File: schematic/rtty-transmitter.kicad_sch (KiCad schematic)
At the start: 32 parts, among them J1 USB_B, J2 USBasp header, J3 Conn_Coaxial, Q1 PN2222A, U1 MCP2221AxP, U2 ATmega328P-P, U3 MCP4901, U4 MCP6022, U5 2x5 Pin Header Connector Fema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, U6 25LC1024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

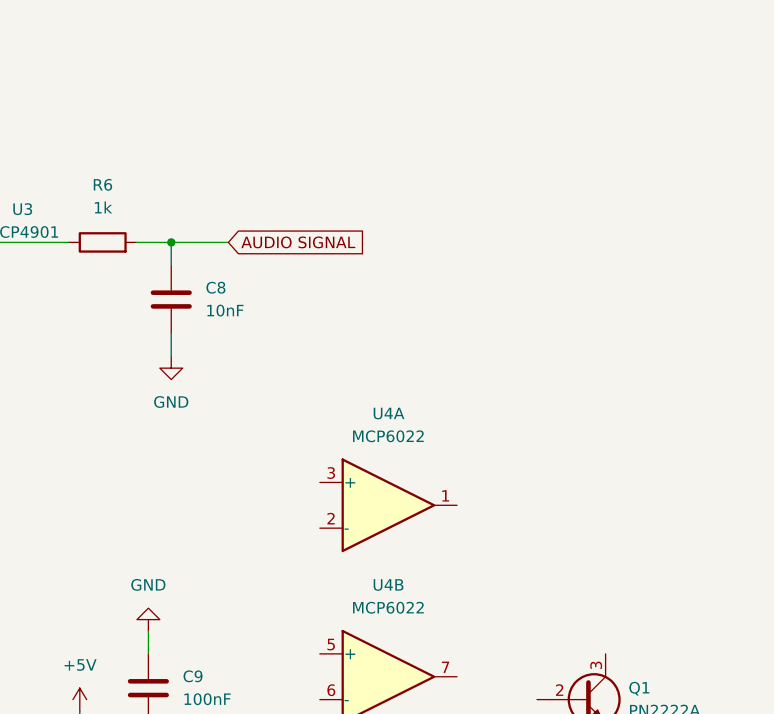
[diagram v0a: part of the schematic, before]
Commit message: High-pass filter added after DAC output to remove DC offset
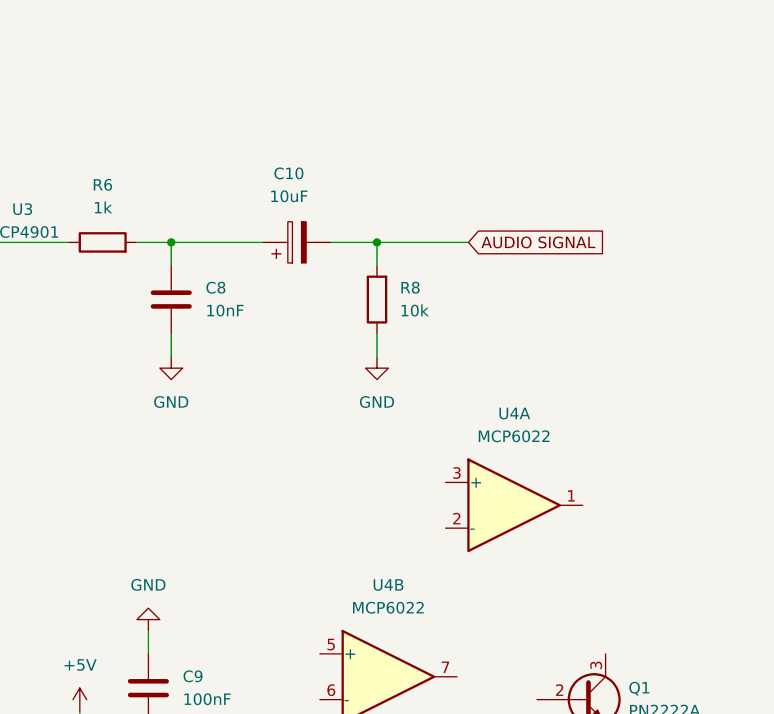
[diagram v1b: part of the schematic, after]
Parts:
- added C10: 10uF, Capacitor_THT:CP_Radial_D6.3mm_P2.50mm, symbol Device:C_Polarized
- added R8: 10k, StockLib:R_10k_Axial_DIN0207, symbol StockLib:R_10k
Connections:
- net AUDIO SIGNAL: now also C10.2, R8.2; no longer C8.2, R6.2
- net GND: now also R8.1
- new net: C10.1, C8.2, R6.2
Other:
- moved on the sheet: U4A
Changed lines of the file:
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@@
   (junction (at 168.91 86.36) (diameter 0) (color 0 0 0 0)
   )
+  (junction (at 245.11 48.26) (diameter 0) (color 0 0 0 0)
+  )
+  (junction (at 222.25 48.26) (diameter 0) (color 0 0 0 0)
+  )
   (junction (at 200.66 109.22) (diameter 0) (color 0 0 0 0)
   )
@@
   )
   (junction (at 182.88 113.03) (diameter 0) (color 0 0 0 0)
-  )
-  (junction (at 222.25 48.26) (diameter 0) (color 0 0 0 0)
   )
   (junction (at 162.56 69.85) (diameter 0) (color 0 0 0 0)
@@
     (stroke (width 0) (type default))
   )
+  (wire (pts (xy 245.11 48.26) (xy 255.27 48.26))
+    (stroke (width 0) (type default))
+  )
   (wire (pts (xy 128.27 123.19) (xy 128.27 125.73))
     (stroke (width 0) (type default))
@@
     (stroke (width 0) (type default))
   )
+  (wire (pts (xy 222.25 48.26) (xy 232.41 48.26))
+    (stroke (width 0) (type default))
+  )
   (wire (pts (xy 143.51 97.79) (xy 151.13 97.79))
     (stroke (width 0) (type default))
@@
     (stroke (width 0) (type default))
   )
-  (wire (pts (xy 222.25 48.26) (xy 228.6 48.26))
-    (stroke (width 0) (type default))
-  )
   (wire (pts (xy 60.96 46.99) (xy 66.04 46.99))
     (stroke (width 0) (type default))
@@
     (stroke (width 0) (type default))
   )
+  (wire (pts (xy 240.03 48.26) (xy 245.11 48.26))
+    (stroke (width 0) (type default))
+  )
   (wire (pts (xy 156.21 59.69) (xy 156.21 48.26))
     (stroke (width 0) (type default))
@@
     (stroke (width 0) (type default))
   )
+  (wire (pts (xy 245.11 48.26) (xy 245.11 50.8))
+    (stroke (width 0) (type default))
+  )
   (wire (pts (xy 193.04 129.54) (xy 193.04 97.79))
     (stroke (width 0) (type default))
@@
   )
   (wire (pts (xy 80.01 114.3) (xy 91.44 114.3))
+    (stroke (width 0) (type default))
+  )
+  (wire (pts (xy 245.11 58.42) (xy 245.11 60.96))
     (stroke (width 0) (type default))
   )
@@
     )
   )
-  (global_label "AUDIO SIGNAL" (shape input) (at 228.6 48.26 0) (fields_autoplaced)
+  (global_label "AUDIO SIGNAL" (shape input) (at 255.27 48.26 0) (fields_autoplaced)
     (effects (font (size 1.27 1.27)) (justify left))
-    (property "Intersheetrefs" "${INTERSHEET_REFS}" (at 244.7087 48.26 0)
+    (property "Intersheetrefs" "${INTERSHEET_REFS}" (at 271.3787 48.26 0)
       (effects (font (size 1.27 1.27)) (justify left) hide)
     )
@@
     )
   )
-  (symbol (lib_id "Amplifier_Operational:MCP6022") (at 246.38 77.47 0) (unit 1)
-    (in_bom yes) (on_board yes) (dnp no) (fields_autoplaced)
-    (property "Reference" "U4" (at 246.38 67.31 0)
-      (effects (font (size 1.27 1.27)))
-    )
-    (property "Value" "MCP6022" (at 246.38 69.85 0)
-      (effects (font (size 1.27 1.27)))
-    )
-    (property "Footprint" "Package_DIP:DIP-8_W7.62mm" (at 246.38 77.47 0)
-      (effects (font (size 1.27 1.27)) hide)
-    )
-    (property "Datasheet" "http://ww1.microchip.com/downloads/en/devicedoc/20001685e.pdf" (at 246.38 77.47 0)
+  (symbol (lib_id "Amplifier_Operational:MCP6022") (at 260.35 77.47 0) (unit 1)
+    (in_bom yes) (on_board yes) (dnp no) (fields_autoplaced)
+    (property "Reference" "U4" (at 260.35 67.31 0)
+      (effects (font (size 1.27 1.27)))
+    )
+    (property "Value" "MCP6022" (at 260.35 69.85 0)
+      (effects (font (size 1.27 1.27)))
+    )
+    (property "Footprint" "Package_DIP:DIP-8_W7.62mm" (at 260.35 77.47 0)
+      (effects (font (size 1.27 1.27)) hide)
+    )
+    (property "Datasheet" "http://ww1.microchip.com/downloads/en/devicedoc/20001685e.pdf" (at 260.35 77.47 0)
       (effects (font (size 1.27 1.27)) hide)
     )
@@
     )
   )
+  (symbol (lib_id "power:GND") (at 245.11 60.96 0) (unit 1)
+    (in_bom yes) (on_board yes) (dnp no) (fields_autoplaced)
+    (property "Reference" "#PWR033" (at 245.11 67.31 0)
+      (effects (font (size 1.27 1.27)) hide)
+    )
+    (property "Value" "GND" (at 245.11 66.04 0)
+      (effects (font (size 1.27 1.27)))
+    )
+    (property "Footprint" "" (at 245.11 60.96 0)
+      (effects (font (size 1.27 1.27)) hide)
+    )
+    (property "Datasheet" "" (at 245.11 60.96 0)
+      (effects (font (size 1.27 1.27)) hide)
+    )
+    (pin "1")
+    (instances
+      (project "rtty-transmitter"
+        (path "/4ea8d87c-4bb0-4c80-84f6-8dbfd2cdcfd6"
+          (reference "#PWR033") (unit 1)
+        )
+      )
+    )
+  )
   (symbol (lib_id "StockLib:LED 5mm YELLOW") (at 62.23 114.3 0) (unit 1)
     (in_bom yes) (on_board yes) (dnp no) (fields_autoplaced)
@@
     )
   )
+  (symbol (lib_id "Device:C_Polarized") (at 236.22 48.26 90) (unit 1)
+    (in_bom yes) (on_board yes) (dnp no) (fields_autoplaced)
+    (property "Reference" "C10" (at 235.331 40.64 90)
+      (effects (font (size 1.27 1.27)))
+    )
+    (property "Value" "10uF" (at 235.331 43.18 90)
+      (effects (font (size 1.27 1.27)))
+    )
+    (property "Footprint" "Capacitor_THT:CP_Radial_D6.3mm_P2.50mm" (at 240.03 47.2948 0)
+      (effects (font (size 1.27 1.27)) hide)
+    )
+    (property "Datasheet" "~" (at 236.22 48.26 0)
+      (effects (font (size 1.27 1.27)) hide)
+    )
+    (pin "1")
+    (pin "2")
+    (instances
+      (project "rtty-transmitter"
+        (path "/4ea8d87c-4bb0-4c80-84f6-8dbfd2cdcfd6"
+          (reference "C10") (unit 1)
+        )
+      )
+    )
+  )
   (symbol (lib_id "power:GND") (at 171.45 45.72 270) (unit 1)
     (in_bom yes) (on_board yes) (dnp no) (fields_autoplaced)
@@
         )
       )
+    )
+  )
+  (symbol (lib_id "StockLib:R_10k") (at 245.11 54.61 180) (unit 1)
+    (in_bom yes) (on_board yes) (dnp no) (fields_autoplaced)
+    (property "Reference" "R8" (at 247.65 53.34 0)
+      (effects (font (size 1.27 1.27)) (justify right))
+    )
+    (property "Value" "10k" (at 247.65 55.88 0)
+      (effects (font (size 1.27 1.27)) (justify right))
+    )
+    (property "Footprint" "StockLib:R_10k_Axial_DIN0207" (at 246.888 54.61 90)
+      (effects (font (size 1.27 1.27)) hide)
+    )
+    (property "Datasheet" "~" (at 245.11 54.61 0)
+      (effects (font (size 1.27 1.27)) hide)
+    )
+    (pin "1")
+    (pin "2")
+    (instances
+      (project "rtty-transmitter"
+        (path "/4ea8d87c-4bb0-4c80-84f6-8dbfd2cdcfd6"
+          (reference "R8") (unit 1)
+        )
+      )

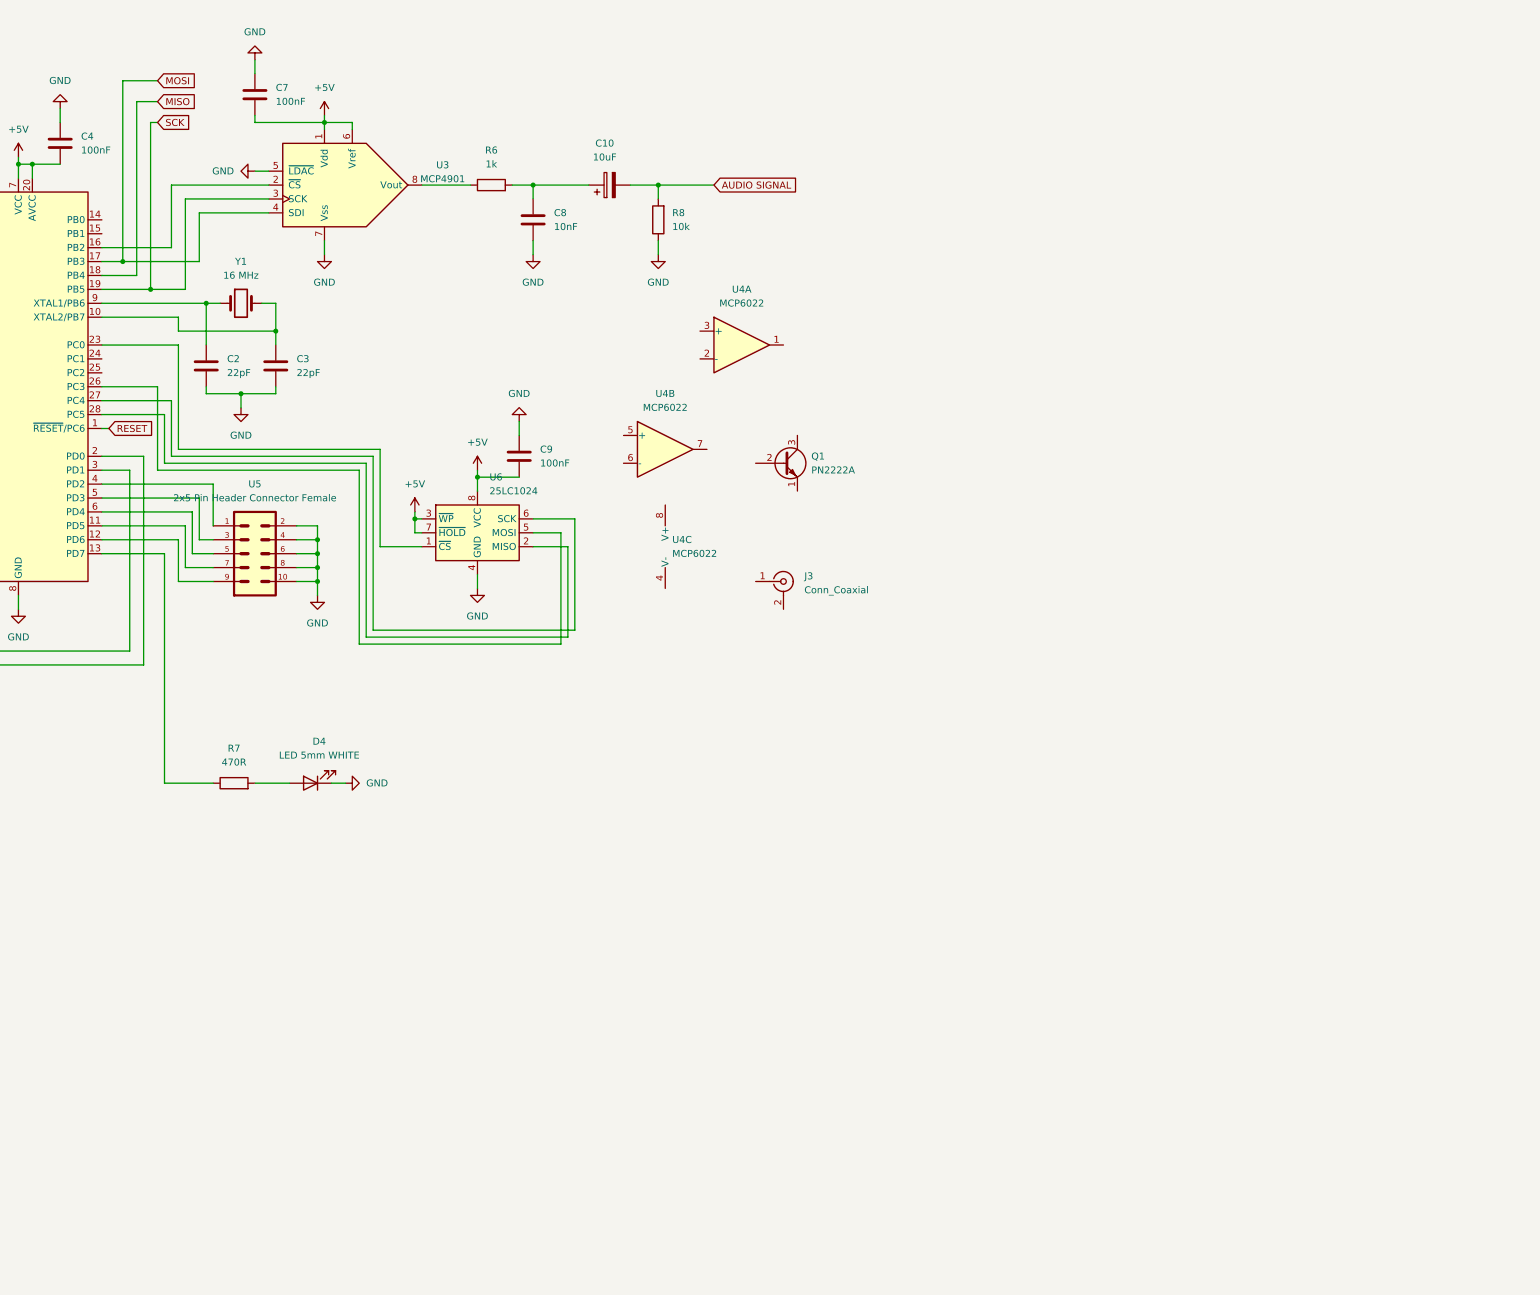
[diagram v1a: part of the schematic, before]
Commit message: Antenna amplifier and modulator-mixer added (current-modulated cascode amplifier), op-amp base circuits added
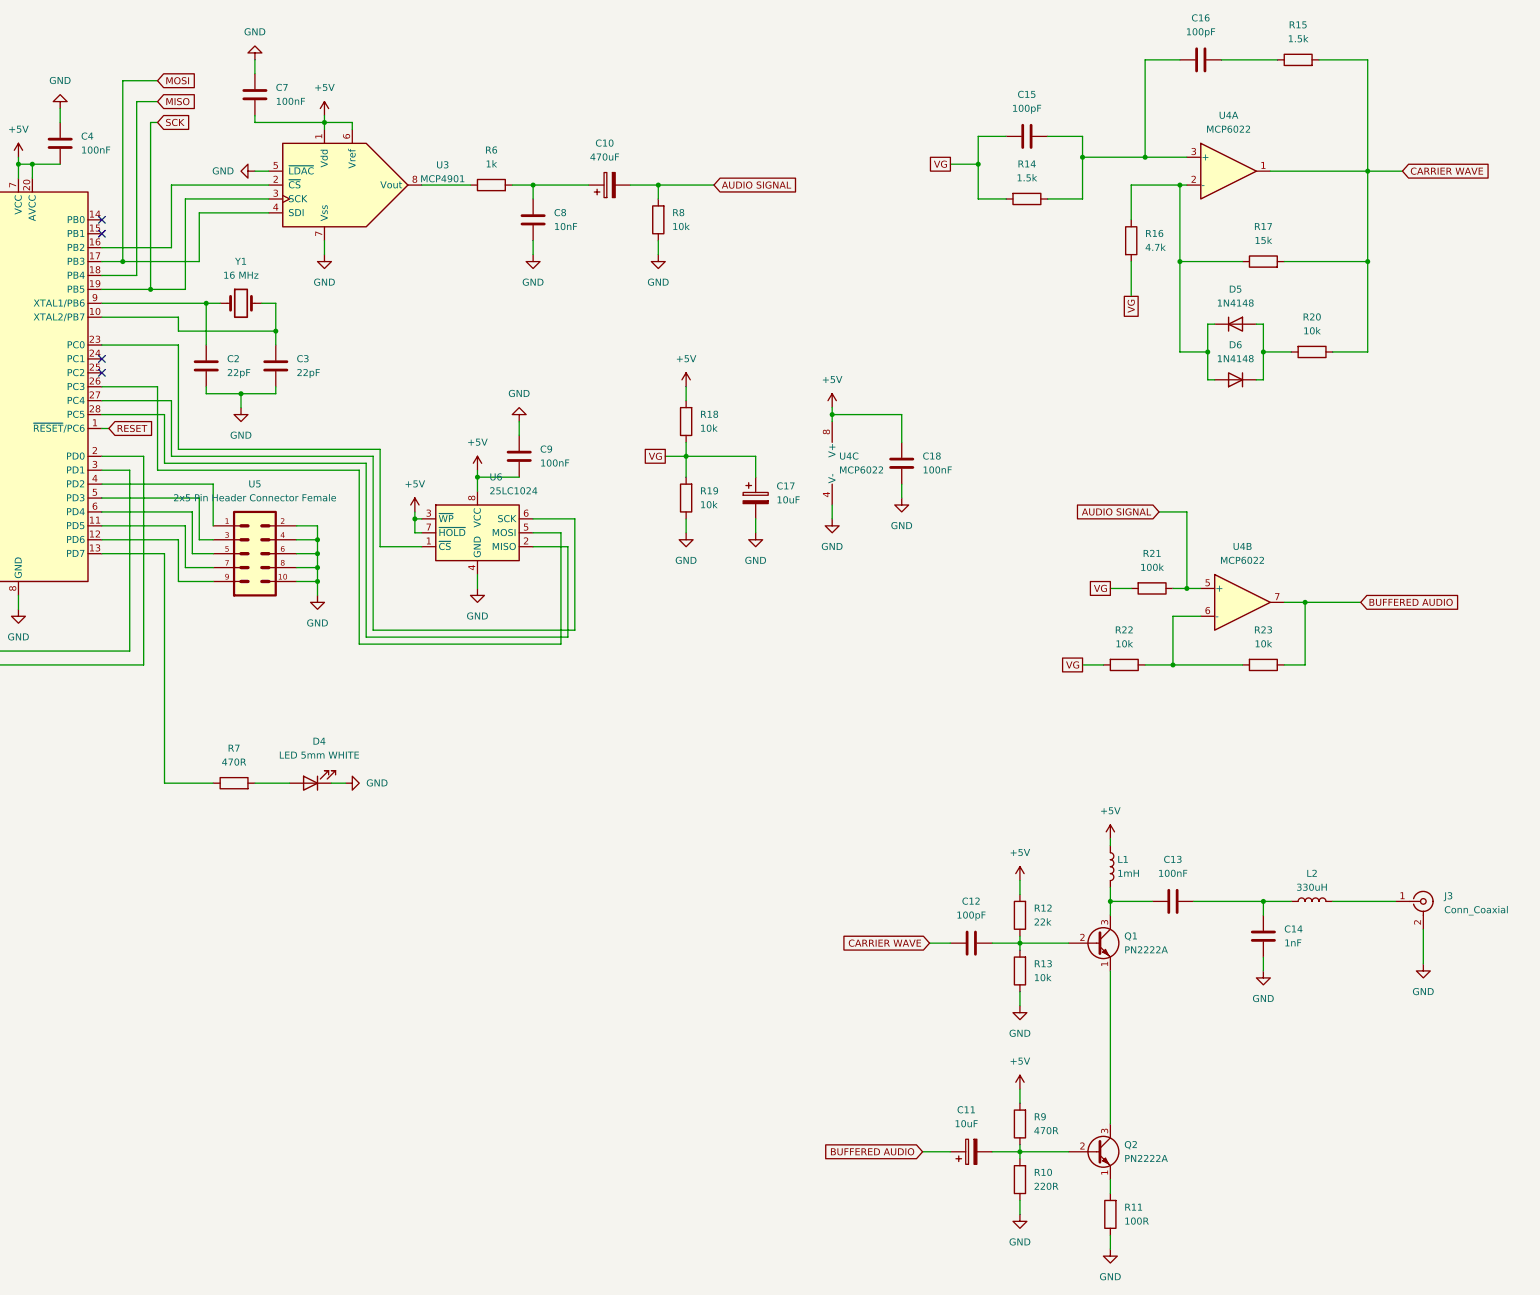
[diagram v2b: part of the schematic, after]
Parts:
- added C11, C17: 10uF, Capacitor_THT:CP_Radial_D6.3mm_P2.50mm, symbol Device:C_Polarized
- added C12, C15, C16: 100pF, Capacitor_THT:C_Disc_D3.0mm_W1.6mm_P2.50mm, symbol Device:C
- added C13, C18: 100nF, StockLib:C_100nF_L7.0mm_W2.5mm_P5.00mm, symbol StockLib:C_100nF
- added C14: 1nF, Capacitor_THT:C_Disc_D3.0mm_W1.6mm_P2.50mm, symbol Device:C
- added D5, D6: 1N4148, Diode_THT:D_DO-35_SOD27_P7.62mm_Horizontal, symbol StockLib:1N4148
- added L1: 1mH, Inductor_THT:L_Radial_D8.7mm_P5.00mm_Fastron_07HCP, symbol StockLib:L
- added L2: 330uH, Inductor_THT:L_Radial_D8.7mm_P5.00mm_Fastron_07HCP, symbol StockLib:L
- added Q2: PN2222A, Package_TO_SOT_THT:TO-92_Inline, symbol StockLib:PN2222A
- added R10: 220R, StockLib:R_10k_Axial_DIN0207, symbol StockLib:R_10k
- added R11: 100R, StockLib:R_10k_Axial_DIN0207, symbol StockLib:R_10k
- added R12: 22k, StockLib:R_10k_Axial_DIN0207, symbol StockLib:R_10k
- added R13, R18, R19, R20, R22, R23: 10k, StockLib:R_10k_Axial_DIN0207, symbol StockLib:R_10k
- added R14, R15: 1.5k, StockLib:R_10k_Axial_DIN0207, symbol StockLib:R_10k
- added R16: 4.7k, StockLib:R_10k_Axial_DIN0207, symbol StockLib:R_10k
- added R17: 15k, StockLib:R_10k_Axial_DIN0207, symbol StockLib:R_10k
- added R21: 100k, StockLib:R_10k_Axial_DIN0207, symbol StockLib:R_10k
- added R9: 470R, StockLib:R_10k_Axial_DIN0207, symbol StockLib:R_10k
- C10: value 10uF -> 470uF
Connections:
- net +5V: now also U4.8 (V+), C18.1, L1.1, R12.2, R18.2, R9.2
- net AUDIO SIGNAL: now also U4.5 (+), R21.1
- net GND: now also J3.2 (Ext), U4.4 (V-), C14.2, C17.2, C18.2, R10.1, R11.1, R13.1, R19.1
- net CARRIER WAVE: now reaches U4.1
- net CARRIER WAVE: now also C12.2, R15.2, R17.2, R20.1
- net at U4.2 (-): now also D5.1 (K), D6.2 (A), R16.1, R17.1
- net at U4.3 (+): now also C15.1, C16.2, R14.1
- net at Q1.1 (E): now also Q2.3 (C)
- net at Q1.2 (B): now also C12.1, R12.1, R13.2
- net at Q1.3 (C): now also C13.1, L1.2
- net at J3.1 (In): now also L2.2
- net at U4.6 (-): now also R22.1, R23.2
- net BUFFERED AUDIO: now reaches U4.7
- net BUFFERED AUDIO: now also C11.1, R23.1
- new net: C11.2, Q2.2 (B), R10.2, R9.1
- new net: Q2.1 (E), R11.2
- new net: C16.1, R15.1
- new net: D5.2 (A), D6.1 (K), R20.2
- new net: C13.2, C14.1, L2.1
- new net VG: C15.2, C17.1, R14.2, R16.2, R18.1, R19.2, R21.2, R22.2
- no-connect marks 9 -> 13
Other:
- moved on the sheet: J3, Q1, U4A, U4B, U4C
